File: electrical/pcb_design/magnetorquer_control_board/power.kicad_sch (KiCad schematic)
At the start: 9 parts, among them J4 External Power, U5 INA260, U6 TLV76733DRVx

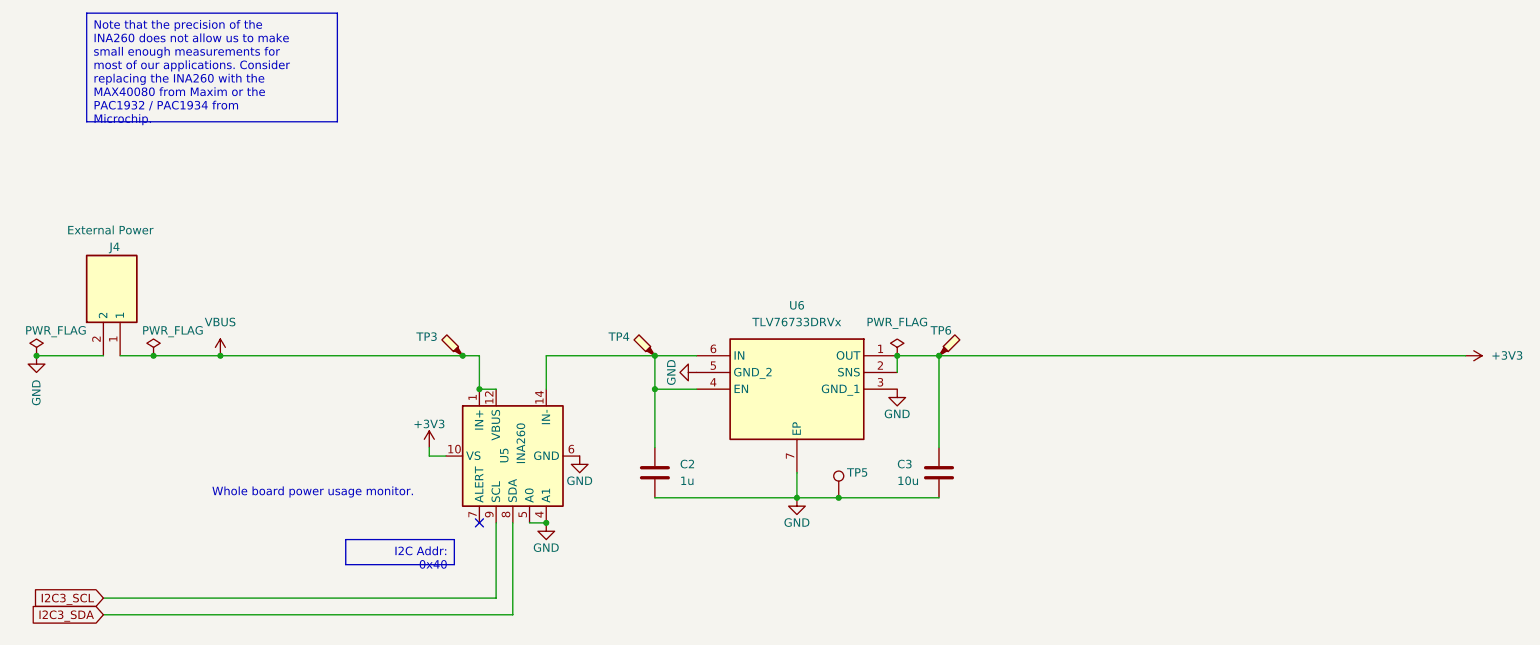
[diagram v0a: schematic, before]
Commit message: Checkpoint progress on magnetorquer control board. All major facilities exist in the schematic. There may be some overlooked details, especially capacitors to reduce noise on power rails. Most of the components are laid out on the schematic, but unconnected.
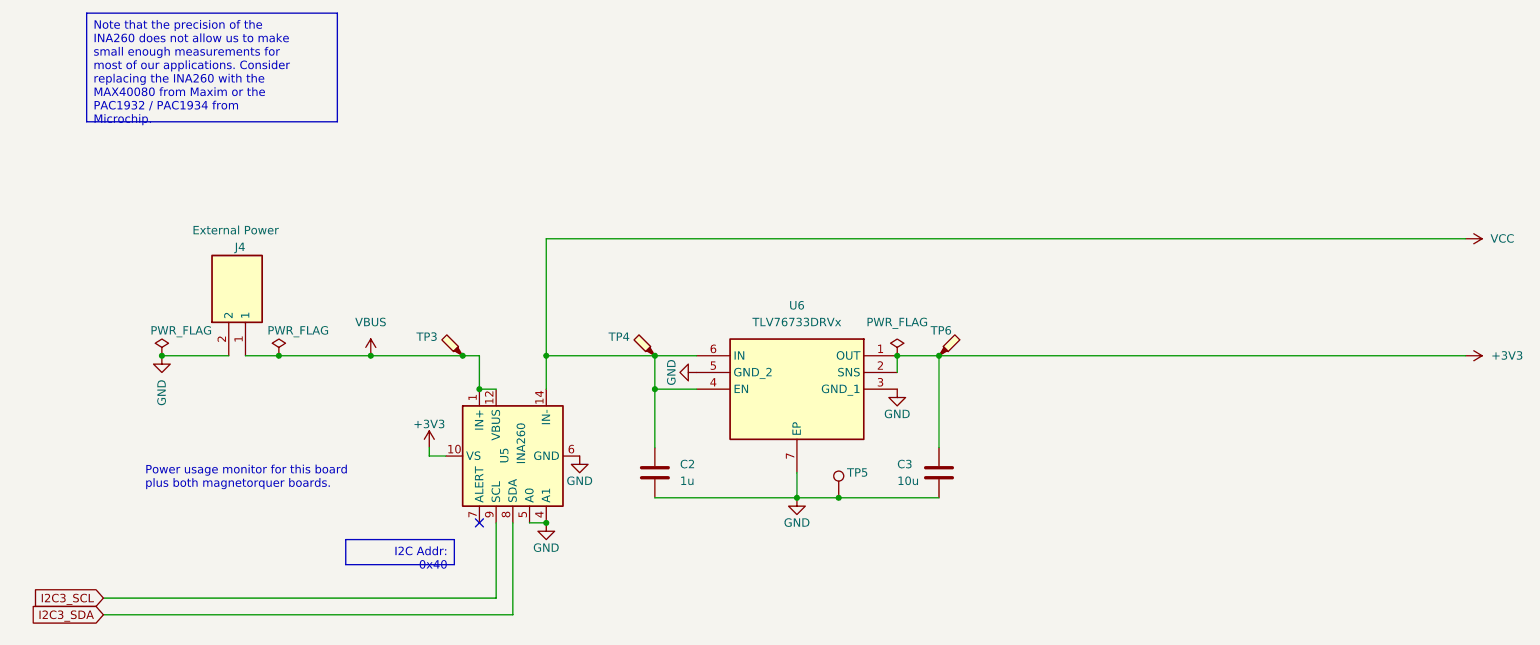
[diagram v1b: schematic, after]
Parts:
- C2, C3, J4, U5, U6: Basic or Extended Component (none) -> Extended
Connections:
- net VCC: now reaches C2.1, TP4.1, U5.14 (IN-), U5.15 (IN-), U5.16 (IN-), U6.4 (EN), U6.6 (IN)
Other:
- note added: "Power usage monitor for this board plus both magnetorquer boards."
- note removed: "Whole board power usage monitor."
- moved on the sheet: J4

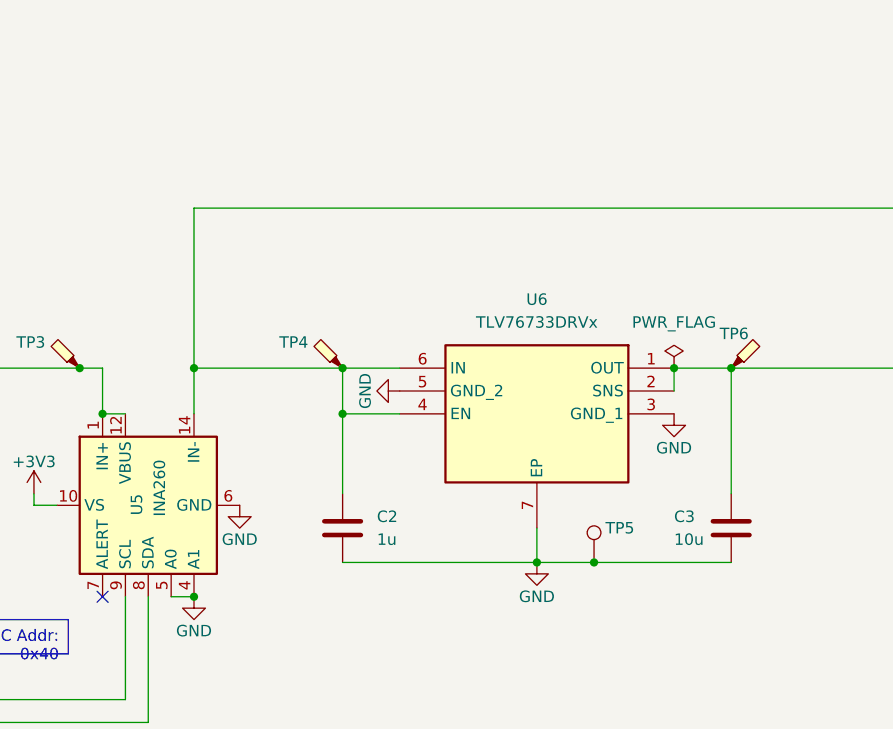
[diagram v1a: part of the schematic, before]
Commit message: Finish routing all traces. Some parts (mostly resistors) still unchosen. Need to audit for JLCPCB Basic vs Extended components to manage cost.
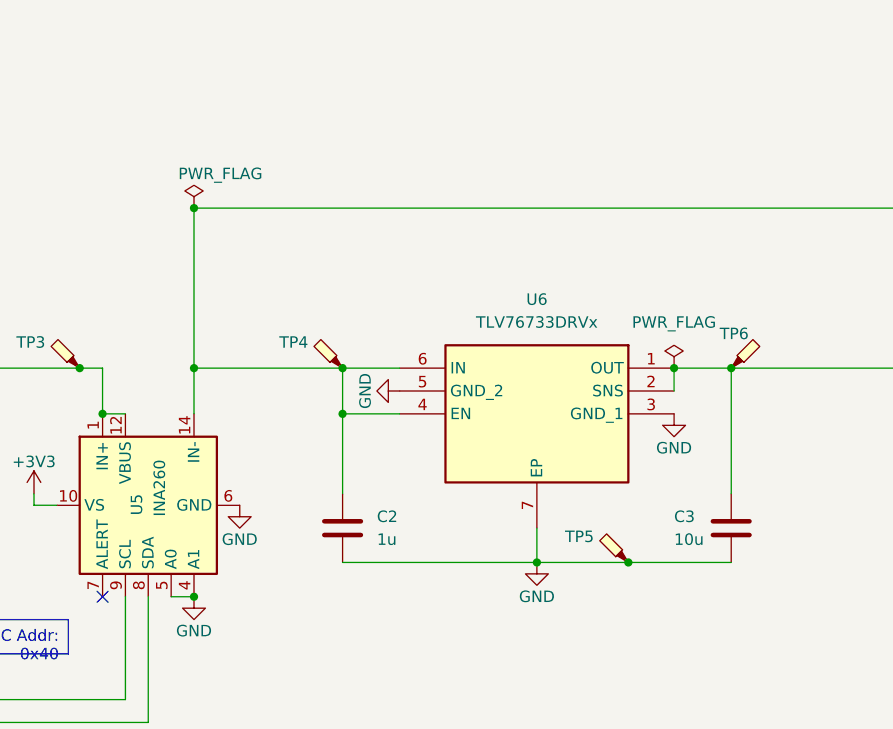
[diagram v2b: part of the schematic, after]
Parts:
- removed TP5: TestPoint_Probe, footprints:TestPoint_Pad_D2.5mm, symbol TVSC:TestPoint_Keystone_5001
- added TP5: TestPoint_Probe, footprints:TestPoint_Pad_D2.5mm, symbol Connector:TestPoint_Probe
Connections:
- net GND: now also TP5.1
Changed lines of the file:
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@@
   (junction (at 111.76 96.52) (diameter 0) (color 0 0 0 0)
   )
-  (junction (at 156.21 92.71) (diameter 0) (color 0 0 0 0)
+  (junction (at 111.76 53.34) (diameter 0) (color 0 0 0 0)
+  )
+  (junction (at 160.02 92.71) (diameter 0) (color 0 0 0 0)
   )
   (junction (at 71.12 71.12) (diameter 0) (color 0 0 0 0)
@@
     (stroke (width 0) (type default))
   )
+  (wire (pts (xy 160.02 92.71) (xy 171.45 92.71))
+    (stroke (width 0) (type default))
+  )
   (wire (pts (xy 101.6 71.12) (xy 101.6 76.2))
     (stroke (width 0) (type default))
   )
-  (wire (pts (xy 156.21 92.71) (xy 171.45 92.71))
-    (stroke (width 0) (type default))
-  )
   (wire (pts (xy 85.09 71.12) (xy 99.06 71.12))
     (stroke (width 0) (type default))
@@
     (stroke (width 0) (type default))
   )
-  (wire (pts (xy 149.86 92.71) (xy 156.21 92.71))
+  (wire (pts (xy 149.86 92.71) (xy 160.02 92.71))
     (stroke (width 0) (type default))
   )
@@
         (path "/695f882b-5312-4493-b26d-8f7d6768a9db/7f8fc7f5-7f1e-476b-9e93-5575de1d6778"
           (reference "#PWR031") (unit 1)
+        )
+      )
+    )
+  )
+  (symbol (lib_id "power:PWR_FLAG") (at 111.76 53.34 0) (unit 1)
+    (in_bom yes) (on_board yes) (dnp no)
+    (property "Reference" "#FLG03" (at 111.76 51.435 0)
+      (effects (font (size 1.27 1.27)) hide)
+    )
+    (property "Value" "PWR_FLAG" (at 119.38 49.53 0)
+      (effects (font (size 1.27 1.27)) (justify right))
+    )
+    (property "Footprint" "" (at 111.76 53.34 0)
+      (effects (font (size 1.27 1.27)) hide)
+    )
+    (property "Datasheet" "~" (at 111.76 53.34 0)
+      (effects (font (size 1.27 1.27)) hide)
+    )
+    (pin "1")
+    (instances
+      (project "magnetorquer_control_board"
+        (path "/695f882b-5312-4493-b26d-8f7d6768a9db/7f8fc7f5-7f1e-476b-9e93-5575de1d6778"
+          (reference "#FLG03") (unit 1)
         )
       )
@@
     )
   )
-  (symbol (lib_id "TVSC:TestPoint_Keystone_5001") (at 156.21 92.71 0) (unit 1)
-    (in_bom yes) (on_board yes) (dnp no)
-    (property "Reference" "TP5" (at 157.48 88.9 0)
-      (effects (font (size 1.27 1.27)) (justify left))
-    )
-    (property "Value" "TestPoint_Probe" (at 158.75 90.678 0)
-      (effects (font (size 1.27 1.27)) (justify left) hide)
-    )
-    (property "Footprint" "footprints:TestPoint_Pad_D2.5mm" (at 161.29 92.71 0)
-      (effects (font (size 1.27 1.27)) hide)
-    )
-    (property "Datasheet" "https://www.keyelco.com/product.cfm/product_id/1310" (at 161.29 92.71 0)
-      (effects (font (size 1.27 1.27)) hide)
-    )
-    (property "Color" "Black" (at 161.29 92.71 0)
-      (effects (font (size 1.27 1.27)) hide)
-    )
-    (property "Manufacturer" "" (at 156.21 92.71 0)
-      (effects (font (size 1.27 1.27)) hide)
-    )
-    (property "Manufacturer Part Number" "" (at 156.21 92.71 0)
-      (effects (font (size 1.27 1.27)) hide)
-    )
-    (property "MPN" "NA" (at 156.21 92.71 0)
-      (effects (font (size 1.27 1.27)) hide)
-    )
-    (property "Active" "Y" (at 156.21 92.71 0)
-      (effects (font (size 1.27 1.27)) hide)
-    )
-    (property "Basic or Extended Component" "" (at 156.21 92.71 0)
-      (effects (font (size 1.27 1.27)) hide)
-    )
-    (pin "1")
-    (instances
-      (project "magnetorquer_control_board"
-        (path "/695f882b-5312-4493-b26d-8f7d6768a9db/7f8fc7f5-7f1e-476b-9e93-5575de1d6778"
-          (reference "TP5") (unit 1)
-        )
-      )
-    )
-  )
   (symbol (lib_id "power:PWR_FLAG") (at 53.34 71.12 0) (unit 1)
     (in_bom yes) (on_board yes) (dnp no)
@@
         )
       )
+    )
+  )
+  (symbol (lib_id "Connector:TestPoint_Probe") (at 160.02 92.71 0) (mirror y) (unit 1)
+    (in_bom yes) (on_board yes) (dnp no)
+    (property "Reference" "TP5" (at 156.21 89.8525 0)
+      (effects (font (size 1.27 1.27)) (justify left))
+    )
+    (property "Value" "TestPoint_Probe" (at 156.21 92.3925 0)
+      (effects (font (size 1.27 1.27)) (justify left) hide)
+    )
+    (property "Footprint" "footprints:TestPoint_Pad_D2.5mm" (at 154.94 92.71 0)
+      (effects (font (size 1.27 1.27)) hide)
+    )
+    (property "Datasheet" "~" (at 154.94 92.71 0)
+      (effects (font (size 1.27 1.27)) hide)
+    )
+    (property "MPN" "NA" (at 160.02 92.71 0)
+      (effects (font (size 1.27 1.27)) hide)
+    )
+    (property "Active" "Y" (at 160.02 92.71 0)
+      (effects (font (size 1.27 1.27)) hide)
+    )
+    (property "Basic or Extended Component" "" (at 160.02 92.71 0)
+      (effects (font (size 1.27 1.27)) hide)
+    )
+    (pin "1")
+    (instances
+      (project "magnetorquer_control_board"
+        (path "/695f882b-5312-4493-b26d-8f7d6768a9db/7f8fc7f5-7f1e-476b-9e93-5575de1d6778"
+          (reference "TP5") (unit 1)
+        )
+      )

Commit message: Swap some capacitors to use JLCPCB Basic parts, rather than Extended parts.
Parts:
- C2: footprint footprints:Nondescript_C_0603_1608Metric -> footprints:Nondescript_C_0402_1005Metric; Basic or Extended Component Extended -> Basic; MPN C77046 -> C52923; Manufacturer Murata Electronics -> Samsung Electro-Mechanics; Manufacturer Part Number GRM188R61E105KA12D -> CL05A105KA5NQNC
- C3: footprint footprints:Nondescript_C_0603_1608Metric -> footprints:Nondescript_C_0402_1005Metric; Basic or Extended Component Extended -> Basic; MPN C344022 -> C15525; Manufacturer Murata Electronics -> Samsung Electro-Mechanics; Manufacturer Part Number GRM188R61E106KA73D -> CL05A106MQ5NUNC
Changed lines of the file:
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@@
       (effects (font (size 1.27 1.27)) (justify left))
     )
-    (property "Footprint" "footprints:Nondescript_C_0603_1608Metric" (at 129.2352 92.71 0)
+    (property "Footprint" "footprints:Nondescript_C_0402_1005Metric" (at 129.2352 92.71 0)
       (effects (font (size 1.27 1.27)) hide)
     )
@@
       (effects (font (size 1.27 1.27)) hide)
     )
-    (property "MPN" "C77046" (at 128.27 88.9 0)
-      (effects (font (size 1.27 1.27)) hide)
-    )
-    (property "Manufacturer" "Murata Electronics" (at 128.27 88.9 0)
-      (effects (font (size 1.27 1.27)) hide)
-    )
-    (property "Manufacturer Part Number" "GRM188R61E105KA12D" (at 128.27 88.9 0)
+    (property "MPN" "C52923" (at 128.27 88.9 0)
+      (effects (font (size 1.27 1.27)) hide)
+    )
+    (property "Manufacturer" "Samsung Electro-Mechanics" (at 128.27 88.9 0)
+      (effects (font (size 1.27 1.27)) hide)
+    )
+    (property "Manufacturer Part Number" "CL05A105KA5NQNC" (at 128.27 88.9 0)
       (effects (font (size 1.27 1.27)) hide)
     )
@@
       (effects (font (size 1.27 1.27)) hide)
     )
-    (property "Basic or Extended Component" "Extended" (at 128.27 88.9 0)
+    (property "Basic or Extended Component" "Basic" (at 128.27 88.9 0)
       (effects (font (size 1.27 1.27)) hide)
     )
@@
       (effects (font (size 1.27 1.27)) (justify left))
     )
-    (property "Footprint" "footprints:Nondescript_C_0603_1608Metric" (at 172.4152 92.71 0)
+    (property "Footprint" "footprints:Nondescript_C_0402_1005Metric" (at 172.4152 92.71 0)
       (effects (font (size 1.27 1.27)) hide)
     )
@@
       (effects (font (size 1.27 1.27)) hide)
     )
-    (property "MPN" "C344022" (at 171.45 88.9 0)
-      (effects (font (size 1.27 1.27)) hide)
-    )
-    (property "Manufacturer" "Murata Electronics" (at 171.45 88.9 0)
-      (effects (font (size 1.27 1.27)) hide)
-    )
-    (property "Manufacturer Part Number" "GRM188R61E106KA73D" (at 171.45 88.9 0)
+    (property "MPN" "C15525" (at 171.45 88.9 0)
+      (effects (font (size 1.27 1.27)) hide)
+    )
+    (property "Manufacturer" "Samsung Electro-Mechanics" (at 171.45 88.9 0)
+      (effects (font (size 1.27 1.27)) hide)
+    )
+    (property "Manufacturer Part Number" "CL05A106MQ5NUNC" (at 171.45 88.9 0)
       (effects (font (size 1.27 1.27)) hide)
     )
@@
       (effects (font (size 1.27 1.27)) hide)
     )
-    (property "Basic or Extended Component" "Extended" (at 171.45 88.9 0)
-      (effects (font (size 1.27 1.27)) hide)
-    )
+    (property "Basic or Extended Component" "Basic" (at 171.45 88.9 0)
+      (effects (font (size 1.27 1.27)) hide)
+    )

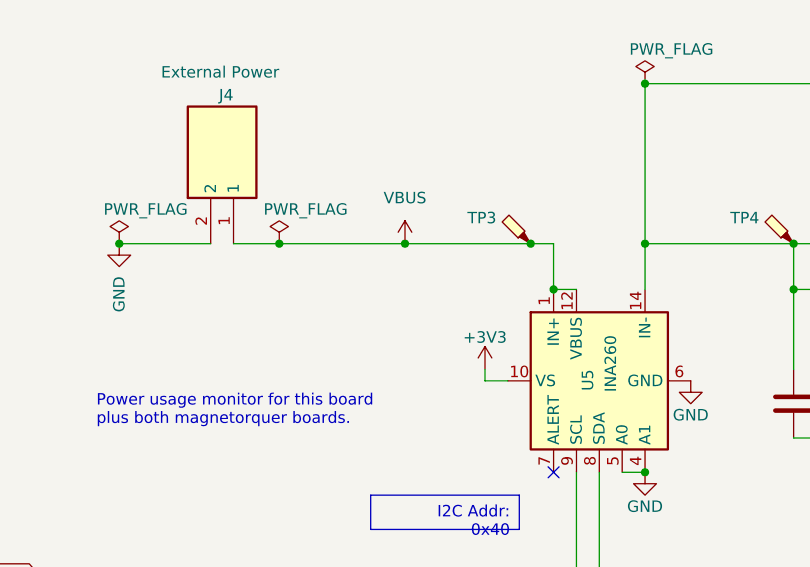
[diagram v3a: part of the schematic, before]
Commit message: Update magnetorquer control board for KiCad 8. Another iteration on schematic, particularly series, pull-up/-down resistors, and decoupling capacitors for SWD, NRST/BOOT0, and SPI.
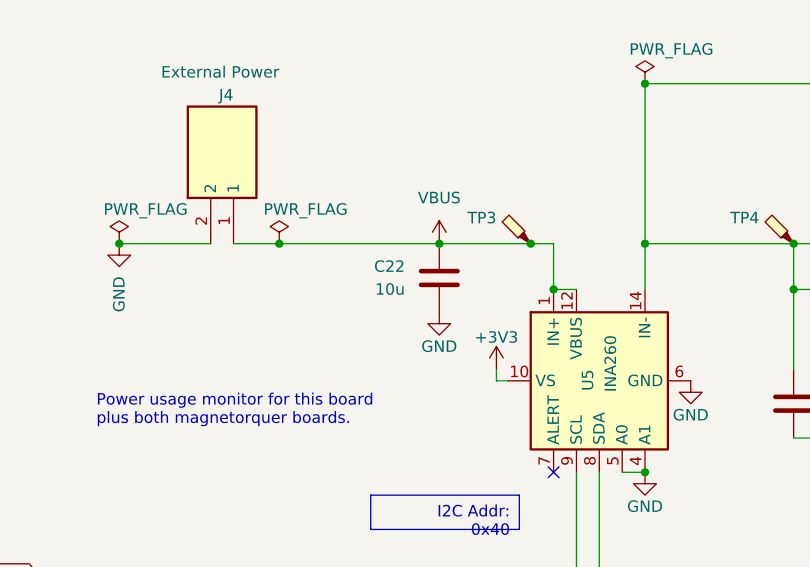
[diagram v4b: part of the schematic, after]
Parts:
- added C22: 10u, footprints:Nondescript_C_0402_1005Metric, symbol Device:C
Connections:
- net GND: now also C22.2
- net VBUS: now also C22.1
